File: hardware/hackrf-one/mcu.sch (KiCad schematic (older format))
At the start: 134 parts, among them J1 USB-MICRO-B, P1 1V8, P20 GPIO, P22 I2S, P23 DBGEN, P24 TRST, P25 LPC_ISP, P26 LPC_JTAG, P28 SD, P29 CPLD_JTAG, P3 GND, P30 BANK2_AUX, P5 LEDS, P68 SPIFI_CS, P69 VREGMODE, P70 EN_1V8, P71 ID, P72 GP_CLKIN, P73 P1_2, P74 P1_1, P75 GP_CLKIN, P76 GP_CLKIN, P77 GP_CLKIN, P78 GP_CLKIN, P79 GP_CLKIN, P8 VCC, P80 SHIELD, P81 SPIFI_SIO2, P82 SPIFI_SIO3, Q5 MOSFET_P, SW1 DFU, SW2 RESET, U15 TVS, U20 W25Q80, U21 TPS62410, U23 LPC4320FBD144, U24 GSG-XC2C64A-7VQG100C, X2 MCU_XTAL, X3 RTC_XTAL

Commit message: HackRF One: replaced NRND GRM155R61A104KA01D 100 nF capacitors with GCM155R71C104KA55
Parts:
- C128, C129, C130, C131, C132, C133, C134, C135, C136, C137, C138, C139, C140, C141, C142, C144, C147, C148, C149, C150, C151, C152, C153, C154: Description CAP CER 0.1UF 10V 10% X5R 0402 -> CAP CER 0.1UF 16V 10% X7R 0402; Part Number GRM155R61A104KA01D -> GCM155R71C104KA55

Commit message: HackRF One: replaced NRND GRM1555C1H330JA01D 33 pF capacitors with GCM1555C1H330JA16
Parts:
- C125: Part Number GRM1555C1H330JA01D -> GCM1555C1H330JA16
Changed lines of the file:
@@
 F 3 "" H 14300 950 60  0001 C CNN
 F 4 "Murata" H 17450 750 60  0001 C CNN "Manufacturer"
-F 5 "GRM1555C1H330JA01D" H 17450 750 60  0001 C CNN "Part Number"
+F 5 "GCM1555C1H330JA16" H 17450 750 60  0001 C CNN "Part Number"
 F 6 "CAP CER 33PF 50V 5% NP0 0402" H 17450 750 60  0001 C CNN "Description"
 	1    14300 950

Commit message: HackRF One: replaced EoL GRM21BR61A106KE19L 10 uF capacitors with GRM21BR61C106KE15
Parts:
- C126, C127, C143, C145, C146: Description CAP CER 10UF 10V 10% X5R 0805 -> CAP CER 10UF 16V 10% X5R 0805; Part Number GRM21BR61A106KE19L -> GRM21BR61C106KE15
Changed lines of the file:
@@
 F 3 "" H 15550 950 60  0001 C CNN
 F 4 "Murata" H 15550 950 60  0001 C CNN "Manufacturer"
-F 5 "GRM21BR61A106KE19L" H 15550 950 60  0001 C CNN "Part Number"
-F 6 "CAP CER 10UF 10V 10% X5R 0805" H 15550 950 60  0001 C CNN "Description"
+F 5 "GRM21BR61C106KE15" H 15550 950 60  0001 C CNN "Part Number"
+F 6 "CAP CER 10UF 16V 10% X5R 0805" H 15550 950 60  0001 C CNN "Description"
 	1    15550 950
 	1    0    0    -1
@@
 F 3 "" H 15550 2450 60  0001 C CNN
 F 4 "Murata" H 15550 2450 60  0001 C CNN "Manufacturer"
-F 5 "GRM21BR61A106KE19L" H 15550 2450 60  0001 C CNN "Part Number"
-F 6 "CAP CER 10UF 10V 10% X5R 0805" H 15550 2450 60  0001 C CNN "Description"
+F 5 "GRM21BR61C106KE15" H 15550 2450 60  0001 C CNN "Part Number"
+F 6 "CAP CER 10UF 16V 10% X5R 0805" H 15550 2450 60  0001 C CNN "Description"
 	1    15550 2450
 	1    0    0    -1
@@
 F 3 "" H 15250 2450 60  0001 C CNN
 F 4 "Murata" H 15250 2450 60  0001 C CNN "Manufacturer"
-F 5 "GRM21BR61A106KE19L" H 15250 2450 60  0001 C CNN "Part Number"
-F 6 "CAP CER 10UF 10V 10% X5R 0805" H 15250 2450 60  0001 C CNN "Description"
+F 5 "GRM21BR61C106KE15" H 15250 2450 60  0001 C CNN "Part Number"
+F 6 "CAP CER 10UF 16V 10% X5R 0805" H 15250 2450 60  0001 C CNN "Description"
 	1    15250 2450
 	1    0    0    -1
@@
 F 3 "" H 15250 950 60  0001 C CNN
 F 4 "Murata" H 15250 950 60  0001 C CNN "Manufacturer"
-F 5 "GRM21BR61A106KE19L" H 15250 950 60  0001 C CNN "Part Number"
-F 6 "CAP CER 10UF 10V 10% X5R 0805" H 15250 950 60  0001 C CNN "Description"
+F 5 "GRM21BR61C106KE15" H 15250 950 60  0001 C CNN "Part Number"
+F 6 "CAP CER 10UF 16V 10% X5R 0805" H 15250 950 60  0001 C CNN "Description"
 	1    15250 950
 	1    0    0    -1
@@
 F 3 "" H 12500 1950 60  0001 C CNN
 F 4 "Murata" H 12500 1950 60  0001 C CNN "Manufacturer"
-F 5 "GRM21BR61A106KE19L" H 12500 1950 60  0001 C CNN "Part Number"
-F 6 "CAP CER 10UF 10V 10% X5R 0805" H 12500 1950 60  0001 C CNN "Description"
+F 5 "GRM21BR61C106KE15" H 12500 1950 60  0001 C CNN "Part Number"
+F 6 "CAP CER 10UF 16V 10% X5R 0805" H 12500 1950 60  0001 C CNN "Description"
 	1    12500 1950
 	1    0    0    -1

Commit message: HackRF One: replaced obsolete NRG4026T4R7M 4.7 uH inductors with NRS4018T4R7MDGJ
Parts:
- L10, L11: Description INDUCTOR 4.7UH 1.6A 20% SMD -> INDUCTOR 4.7UH 1.7A 20% SMD; Part Number NRG4026T4R7M -> NRS4018T4R7MDGJ
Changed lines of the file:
@@
 F 3 "" H 15050 2300 60  0001 C CNN
 F 4 "Taiyo Yuden" V 15050 2300 60  0001 C CNN "Manufacturer"
-F 5 "NRG4026T4R7M" V 15050 2300 60  0001 C CNN "Part Number"
-F 6 "INDUCTOR 4.7UH 1.6A 20% SMD" V 15050 2300 60  0001 C CNN "Description"
+F 5 "NRS4018T4R7MDGJ" V 15050 2300 60  0001 C CNN "Part Number"
+F 6 "INDUCTOR 4.7UH 1.7A 20% SMD" V 15050 2300 60  0001 C CNN "Description"
 	1    15050 2300
 	-1   0    0    1
@@
 F 3 "" H 15050 1100 60  0001 C CNN
 F 4 "Taiyo Yuden" V 15050 1100 60  0001 C CNN "Manufacturer"
-F 5 "NRG4026T4R7M" V 15050 1100 60  0001 C CNN "Part Number"
-F 6 "INDUCTOR 4.7UH 1.6A 20% SMD" V 15050 1100 60  0001 C CNN "Description"
+F 5 "NRS4018T4R7MDGJ" V 15050 1100 60  0001 C CNN "Part Number"
+F 6 "INDUCTOR 4.7UH 1.7A 20% SMD" V 15050 1100 60  0001 C CNN "Description"
 	1    15050 1100
 	-1   0    0    1

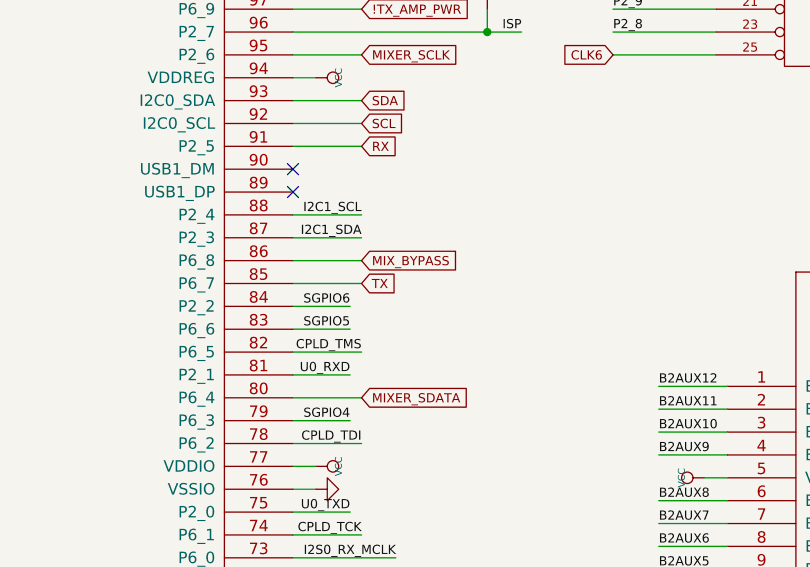
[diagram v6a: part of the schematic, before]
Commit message: HackRF One: replaced EoL SKY13350-385LF RF switch with SKY13453-385LF
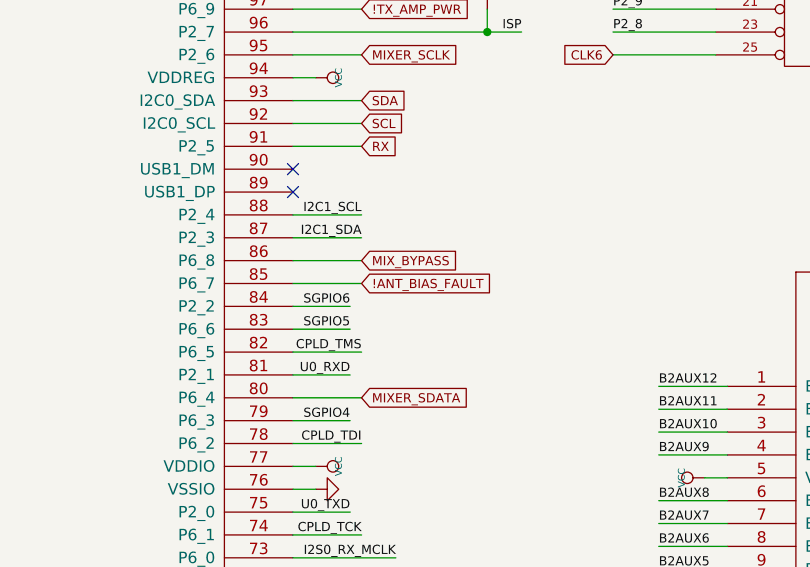
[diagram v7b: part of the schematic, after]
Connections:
- net TX renamed !ANT_BIAS_FAULT
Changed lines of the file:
@@
 	1    0    0    -1
 $EndComp
-Text GLabel 10000 5300 2    40   Input ~ 0
-TX
 Text GLabel 4200 3000 0    40   Input ~ 0
 HP
@@
 	9700 5200 10000 5200
 Wire Wire Line
-	10000 5300 9700 5300
-Wire Wire Line
 	7850 7450 7850 7750
 Wire Wire Line
@@
 Wire Wire Line
 	1700 7900 1700 8000
+Text GLabel 10000 5300 2    40   Input ~ 0
+!ANT_BIAS_FAULT
+Wire Wire Line
+	9700 5300 10000 5300
 $EndSCHEMATC

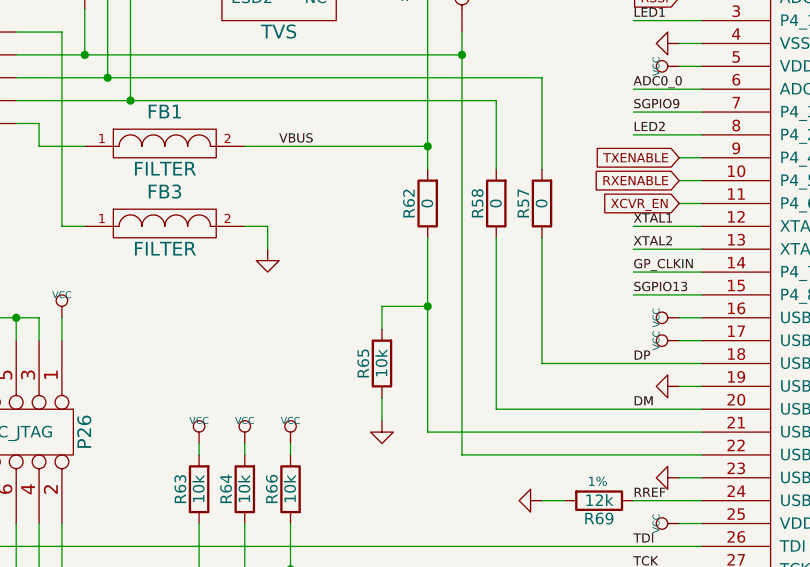
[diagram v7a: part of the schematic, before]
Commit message: HackRF One: changed VBUS voltage divider to match GreatFET One
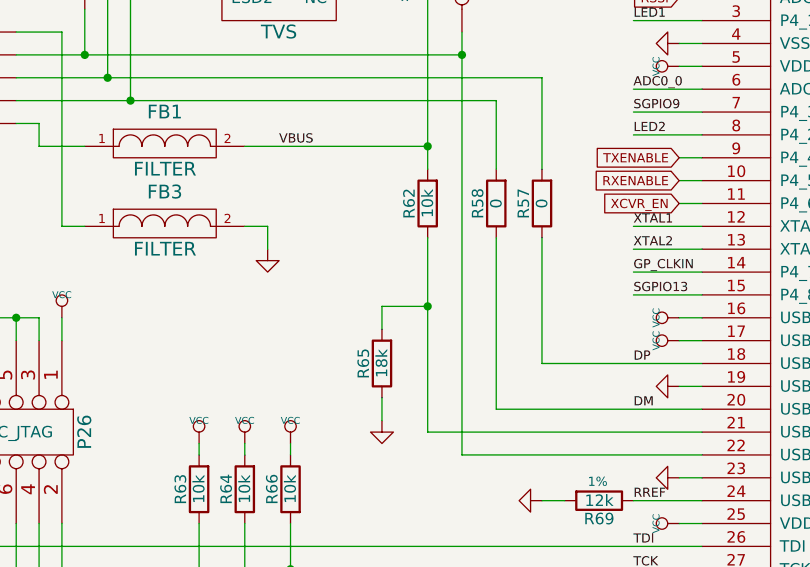
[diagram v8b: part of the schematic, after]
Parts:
- R62: value 0 -> 10k; Description RES 0.0 OHM 1/16W 0402 SMD -> RES 10K OHM 1/16W 5% 0402 SMD; Part Number RMCF0402ZT0R00 -> RMCF0402JT10K0
- R65: value 10k -> 18k; Description RES 10K OHM 1/16W 5% 0402 SMD -> RES SMD 18K OHM 5% 1/10W 0603; Manufacturer Stackpole -> Yageo; Part Number RMCF0402JT10K0 -> RC0603JR-0718KL
